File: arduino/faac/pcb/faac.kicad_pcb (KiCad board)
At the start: 2 copper layers, 31.7 x 50 mm, 5 parts, among them J1 BatCon, U1 HPD8407-F, U2 ProMini, U3 Reg3V3

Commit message: faac: Add labels
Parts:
- removed AE1: ANT, myfoots:antenna
- removed U1: HPD8407-F, myfoots:HPD8407-F
- added ANT: ANT, myfoots:antenna, F.Cu at (115.2, 126.9)
- added HPD8407F: HPD8407-F, myfoots:HPD8407-F, F.Cu at (111.5, 121.0)
- PRO MINI: renamed from U2
- renumbered J1 to BAT, U3 to REG
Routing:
- added copper zone on B.Cu, net GND
- added copper zone on F.Cu, net GND
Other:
- board text added: "+"
- board text added: "-"
- board text added: "3V3"
- board text added: "ANT"
- board text added: "DA"
- board text added: "FAAC v1.0"
- board text added: "GND"
- board text added: "VBAT"
- board text added: "github.com/tantecky/embedded"
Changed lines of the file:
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@@
-(kicad_pcb (version 20171130) (host pcbnew 5.0.2-bee76a0~70~ubuntu18.04.1)
+(kicad_pcb (version 20171130) (host pcbnew "(5.0.2)-1")
   (general
     (thickness 1.6)
-    (drawings 4)
+    (drawings 22)
     (tracks 16)
     (zones 0)
@@
   (page A4)
   (layers
-    (0 F.Cu signal)
-    (31 B.Cu signal)
+    (0 F.Cu signal hide)
+    (31 B.Cu signal hide)
     (32 B.Adhes user)
     (33 F.Adhes user)
     (34 B.Paste user)
     (35 F.Paste user)
-    (36 B.SilkS user)
+    (36 B.SilkS user hide)
     (37 F.SilkS user)
     (38 B.Mask user)
@@
   (module myfoots:antenna (layer F.Cu)
     (at 115.24 126.94)
-    (fp_text reference AE1 (at -3.683 0) (layer F.SilkS)
-      (effects (font (size 1 1) (thickness 0.15)))
+    (fp_text reference ANT (at -3.226 -0.067) (layer F.SilkS)
+      (effects (font (size 1.2 1.2) (thickness 0.2)))
     )
     (fp_text value ANT (at 0.127 5.08) (layer F.Fab)
@@
   (module myfoots:BatCon (layer F.Cu)
     (at 112.522 100.33 270)
-    (fp_text reference J1 (at 2.54 4.572 270) (layer F.SilkS)
-      (effects (font (size 1 1) (thickness 0.2)))
+    (fp_text reference BAT (at 4.445 5.461) (layer F.SilkS)
+      (effects (font (size 1.2 1.2) (thickness 0.2)))
     )
     (fp_text value BatCon (at 0 10.922 270) (layer F.Fab)
@@
   (module myfoots:HPD8407-F (layer F.Cu)
     (at 111.493 121.027)
-    (fp_text reference U1 (at -4.953 1.143) (layer F.SilkS)
-      (effects (font (size 1 1) (thickness 0.2)))
+    (fp_text reference HPD8407F (at 0.013 1.274) (layer F.SilkS)
+      (effects (font (size 1.2 1.2) (thickness 0.2)))
     )
     (fp_text value HPD8407-F (at -13.843 -9.017) (layer F.Fab)
@@
   (module myfoots:ProMini (layer F.Cu)
     (at 127 128.24)
-    (fp_text reference U2 (at -11.43 -5.08) (layer F.SilkS)
-      (effects (font (size 1 1) (thickness 0.2)))
+    (fp_text reference "PRO MINI" (at 0 -1.367) (layer F.SilkS)
+      (effects (font (size 1.2 1.2) (thickness 0.2)))
     )
     (fp_text value ProMini (at 13.97 -1.27) (layer F.Fab)
@@
   (module myfoots:Reg3V3 (layer F.Cu)
     (at 124.536 80.826 180)
-    (fp_text reference U3 (at 14.097 1.016 180) (layer F.SilkS)
+    (fp_text reference REG (at 13.538 0.689 180) (layer F.SilkS)
       (effects (font (size 1 1) (thickness 0.2)))
     )
@@
     (pad 1 thru_hole rect (at 2.54 0 180) (size 2 2) (drill 1) (layers *.Cu *.Mask)
       (net 5 "Net-(U1-Pad2)"))
+  )
+  (gr_text github.com/tantecky/embedded (at 106.045 88.646 90) (layer F.SilkS)
+    (effects (font (size 0.76 0.76) (thickness 0.15)))
+  )
+  (gr_text "FAAC v1.0" (at 108.204 87.249 90) (layer F.SilkS)
+    (effects (font (size 1.5 1.5) (thickness 0.3)))
+  )
+  (gr_text GND (at 108.839 102.743) (layer B.SilkS)
+    (effects (font (size 1.2 1.2) (thickness 0.2)) (justify mirror))
+  )
+  (gr_text VBAT (at 108.585 97.79) (layer B.SilkS)
+    (effects (font (size 1.2 1.2) (thickness 0.2)) (justify mirror))
+  )
+  (gr_text ANT (at 112.014 127) (layer B.SilkS)
+    (effects (font (size 1.2 1.2) (thickness 0.2)) (justify mirror))
+  )
+  (gr_text ANT (at 115.316 117.094) (layer B.SilkS)
+    (effects (font (size 1.2 1.2) (thickness 0.2)) (justify mirror))
+  )
+  (gr_text 3V3 (at 110.236 117.221) (layer B.SilkS)
+    (effects (font (size 1.2 1.2) (thickness 0.2)) (justify mirror))
+  )
+  (gr_text VBAT (at 110.617 80.772) (layer B.SilkS)
+    (effects (font (size 1.2 1.2) (thickness 0.2)) (justify mirror))
+  )
+  (gr_text 3V3 (at 122.047 83.185) (layer B.SilkS)
+    (effects (font (size 1.2 1.2) (thickness 0.2)) (justify mirror))
+  )
+  (gr_text GND (at 118.11 83.185) (layer B.SilkS)
+    (effects (font (size 1.2 1.2) (thickness 0.2)) (justify mirror))
+  )
+  (gr_text DA (at 122.174 99.06) (layer B.SilkS)
+    (effects (font (size 1.2 1.2) (thickness 0.2)) (justify mirror))
+  )
+  (gr_text 3V3 (at 122.682 116.967) (layer B.SilkS)
+    (effects (font (size 1.2 1.2) (thickness 0.2)) (justify mirror))
+  )
+  (gr_text GND (at 122.682 121.92) (layer B.SilkS)
+    (effects (font (size 1.2 1.2) (thickness 0.2)) (justify mirror))
+  )
+  (gr_text GND (at 131.318 116.84) (layer B.SilkS)
+    (effects (font (size 1.2 1.2) (thickness 0.2)) (justify mirror))
+  )
+  (gr_text GND (at 107.696 122.301) (layer B.SilkS)
+    (effects (font (size 1.2 1.2) (thickness 0.2)) (justify mirror))
+  )
+  (gr_text - (at 108.077 102.87) (layer F.SilkS)
+    (effects (font (size 1.2 1.2) (thickness 0.2)))
+  )
+  (gr_text + (at 108.077 97.79) (layer F.SilkS)
+    (effects (font (size 1.2 1.2) (thickness 0.2)))
+  )
+  (gr_text DA (at 112.776 122.301) (layer B.SilkS)
+    (effects (font (size 1.2 1.2) (thickness 0.2)) (justify mirror))
   )
   (gr_line (start 105 78.9) (end 105 128.9) (layer Edge.Cuts) (width 0.15))
@@
   (segment (start 122.047 81.026) (end 122.047 82.788) (width 0.762) (layer B.Cu) (net 5))
   (segment (start 110.49 117.618) (end 110.49 119.38) (width 0.762) (layer B.Cu) (net 5))
+  (zone (net 3) (net_name GND) (layer F.Cu) (hatch edge 0.508)
+    (connect_pads (clearance 0.508))
+    (min_thickness 0.254)
+    (fill yes (arc_segments 16) (thermal_gap 0.508) (thermal_bridge_width 0.508))
+    (polygon
+      (pts
+        (xy 105.41 79.248) (xy 136.271 79.248) (xy 136.271 128.651) (xy 105.41 128.651)
+      )
+    )
+  )
+  (zone (net 3) (net_name GND) (layer B.Cu) (hatch edge 0.508)
+    (connect_pads (clearance 0.508))
+    (min_thickness 0.254)
+    (fill yes (arc_segments 16) (thermal_gap 0.508) (thermal_bridge_width 0.508))
+    (polygon
+      (pts
+        (xy 105.41 79.248) (xy 136.398 79.248) (xy 136.398 128.651) (xy 105.41 128.651)
+      )
+    )
+  )
 )

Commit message: faac: Add a logo
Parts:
- added ?: , myfoots:logo, F.Cu at (108.8, 92.6)

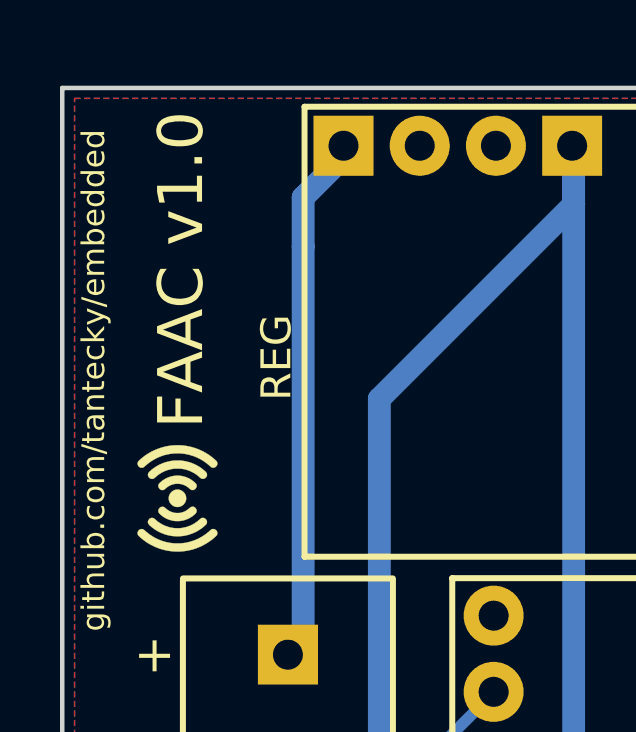
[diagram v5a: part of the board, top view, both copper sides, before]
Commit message: faac: Send to a fab (JLPCB)
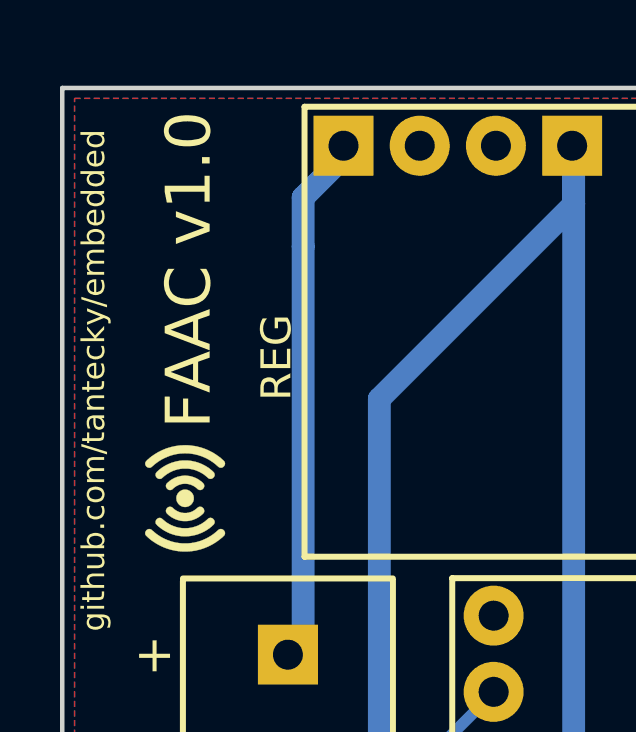
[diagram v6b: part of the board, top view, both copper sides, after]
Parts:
- moved ? 0.25 mm to (109.1, 92.6)
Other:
- board text added: "0V9-6V"
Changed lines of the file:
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@@
   (general
     (thickness 1.6)
-    (drawings 22)
+    (drawings 23)
     (tracks 16)
     (zones 0)
@@
   (page A4)
   (layers
-    (0 F.Cu signal hide)
-    (31 B.Cu signal hide)
+    (0 F.Cu signal)
+    (31 B.Cu signal)
     (32 B.Adhes user)
     (33 F.Adhes user)
-    (34 B.Paste user)
+    (34 B.Paste user hide)
     (35 F.Paste user)
     (36 B.SilkS user hide)
@@
     (47 F.CrtYd user)
     (48 B.Fab user)
-    (49 F.Fab user)
+    (49 F.Fab user hide)
   )
   (setup
@@
     (visible_elements 7FFFFFFF)
     (pcbplotparams
-      (layerselection 0x010fc_ffffffff)
+      (layerselection 0x010f0_ffffffff)
       (usegerberextensions false)
       (usegerberattributes false)
@@
       (outputformat 1)
       (mirror false)
-      (drillshape 1)
+      (drillshape 0)
       (scaleselection 1)
-      (outputdirectory ""))
+      (outputdirectory "gerbs/"))
   )
   (net 0 "")
@@
   )
   (module myfoots:logo (layer F.Cu)
-    (at 108.839 92.583 90)
+    (at 109.093 92.583 90)
     (fp_text reference "" (at 0 0 90) (layer F.SilkS)
       (effects (font (size 1.27 1.27) (thickness 0.15)))
@@
       (xy -1.188747 -1.325353) (xy -1.178099 -1.327368) (xy -1.151258 -1.328552) (xy -1.124183 -1.3238)) (layer F.SilkS) (width 0.01))
   )
+  (gr_text 0V9-6V (at 110.236 95.377) (layer B.SilkS)
+    (effects (font (size 1.2 1.2) (thickness 0.2)) (justify mirror))
+  )
   (gr_text github.com/tantecky/embedded (at 106.045 88.646 90) (layer F.SilkS)
     (effects (font (size 0.76 0.76) (thickness 0.15)))
   )
-  (gr_text "FAAC v1.0" (at 108.966 84.963 90) (layer F.SilkS)
+  (gr_text "FAAC v1.0" (at 109.22 84.963 90) (layer F.SilkS)
     (effects (font (size 1.5 1.5) (thickness 0.3)))
   )
